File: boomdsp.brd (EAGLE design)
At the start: 100 x 100 mm, 25 parts, among them J1 RCA, J2 RCA

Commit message: proto
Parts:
- removed C1, C2: 2.2nF 50V, rcl:C025-030X050
- removed GPIO: 1X4, headers(2mm):1X4
- removed J1, J2: RCA, SparkFun-Connectors:RCA
- added OUTL, OUTR: 1X2, headers(2mm):1X2
- added U$3: 1X5, headers(2mm):1X5
- moved C14 39.5 mm to (22.5, 4.50)
- moved C13 18.7 mm to (8.50, 4.50), turned to 180 degrees
- moved R1 3.00 mm to (13.5, 9.00)
- moved C5 1.00 mm to (14.5, 13.0)
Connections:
- new net N$21: U$1.25, U$3.5
- net GND: now also C13.2, C14.2, OUTL.1, OUTR.2; no longer C1.2, C2.2
- net N$10: now also U$3.3; no longer GPIO.3
- net N$11: now also U$3.1; no longer GPIO.1
- net N$3: now also C14.1, OUTR.1; no longer C2.1
- net N$4: now also C13.1, OUTL.2; no longer C1.1
- net N$7: now also U$3.2; no longer GPIO.2
- net N$8: now also U$3.4; no longer GPIO.4
- net VDD: no longer U$1.25
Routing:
- net N$10: track 7.16 -> 1.86 mm
- net N$8: track 4.97 -> 0.60 mm
- net N$11: track 7.60 -> 4.06 mm
- net N$7: track 3.83 -> 1.32 mm
- net N$1: track 7.44 -> 9.83 mm
- net N$4: track 5.70 -> 3.55 mm
- net N$3: track 5.70 -> 3.71 mm
- net VDD: track 12.4 -> 11.3 mm

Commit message: finished prototype
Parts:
- removed C10, C11: 1uF, rcl:C0805
- removed C12: (no value), rcl:C0603K
- removed C9: 10uF 16V, rcl:153CLV-0405
- removed LED1: (no value), led:LED3MM
- removed U$3: 1X5, headers(2mm):1X5
- added C1: (no value), rcl:E3,5-8
- added POWER1: 1X2, headers(2mm):1X2
- added U$4: 1X1, headers(2mm):1X1
- U$2: value LP5907 -> 1X4; device boomdsp:SOT23-6 -> headers(2mm):1X4
- moved U$2 18.8 mm to (23.0, 26.5), turned to 270 degrees
- moved C4 5.83 mm to (7.50, 27.0)
- moved C3 5.00 mm to (11.5, 28.0)
- moved C5 4.24 mm to (11.5, 16.0)
- moved C6 4.24 mm to (9.50, 21.0)
- moved C7 4.24 mm to (11.5, 18.0)
- moved I2C 4.24 mm to (23.0, 20.5)
- moved I2S 4.24 mm to (17.5, 31.0)
- moved R1 4.24 mm to (10.5, 12.0)
- moved R2 4.24 mm to (15.5, 12.0)
- moved U$1 4.24 mm to (15.7, 22.8)
- moved C8 3.91 mm to (18.0, 16.5)
- moved C13 2.24 mm to (7.50, 6.50)
- moved OUTL 2.06 mm to (11.5, 3.00)
- moved OUTR 2.06 mm to (18.5, 3.00)
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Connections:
- removed net +5V: C10.1, POWER.1, U$2.1, U$2.3
- removed net VDD: C4.1, U$1.18, U$1.28
- net GND: now also C1.-, POWER1.2, U$1.16, U$1.24; no longer C10.2, C11.2, C9.-, U$2.2
- net N$10: now also U$2.3; no longer U$3.3
- net N$11: now also U$2.1; no longer U$3.1
- net N$15: now also C1.+; no longer C9.+
- net N$21: now also U$4.1; no longer U$3.5
- net N$7: now also U$2.2; no longer U$3.2
- net N$8: now also U$2.4; no longer U$3.4
- net VCC: now also C4.1, POWER.1, POWER1.1, U$1.18, U$1.28; no longer C11.1, U$2.6
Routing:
- net VCC: track 20.8 -> 39.2 mm
- net +5V: track 18.2 -> 0.00 mm
- net VDD: track 11.3 -> 0.00 mm
- net N$21: track 0.00 -> 6.10 mm
- net N$10: track 1.86 -> 7.16 mm
- net N$4: track 3.55 -> 8.74 mm
- net N$3: track 3.71 -> 8.68 mm
- net N$8: track 0.60 -> 4.97 mm
- net N$11: track 4.06 -> 7.60 mm
- net GND: track 7.82 -> 4.34 mm
- net N$7: track 1.32 -> 3.83 mm
- net N$15: track 6.88 -> 9.00 mm
- added copper zone on layer 16, net GND

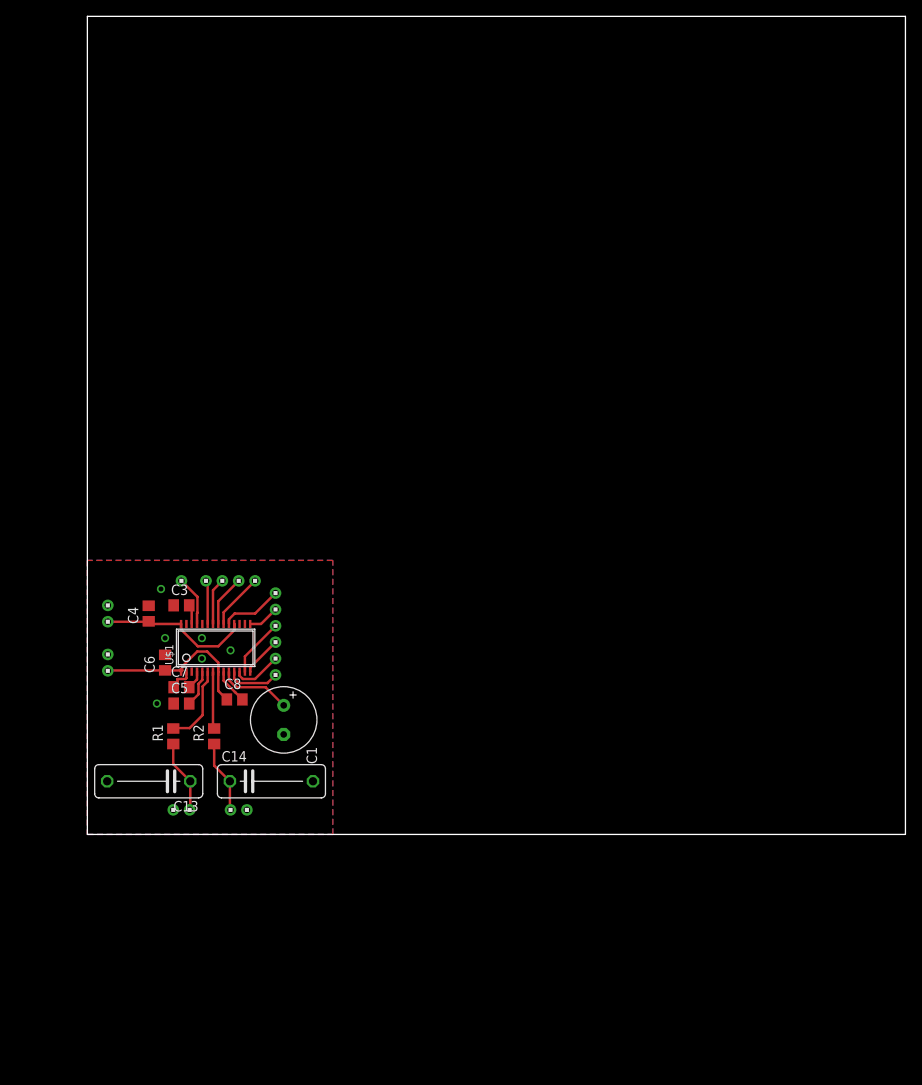
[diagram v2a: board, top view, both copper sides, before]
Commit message: via under chip. doesnt work for diy
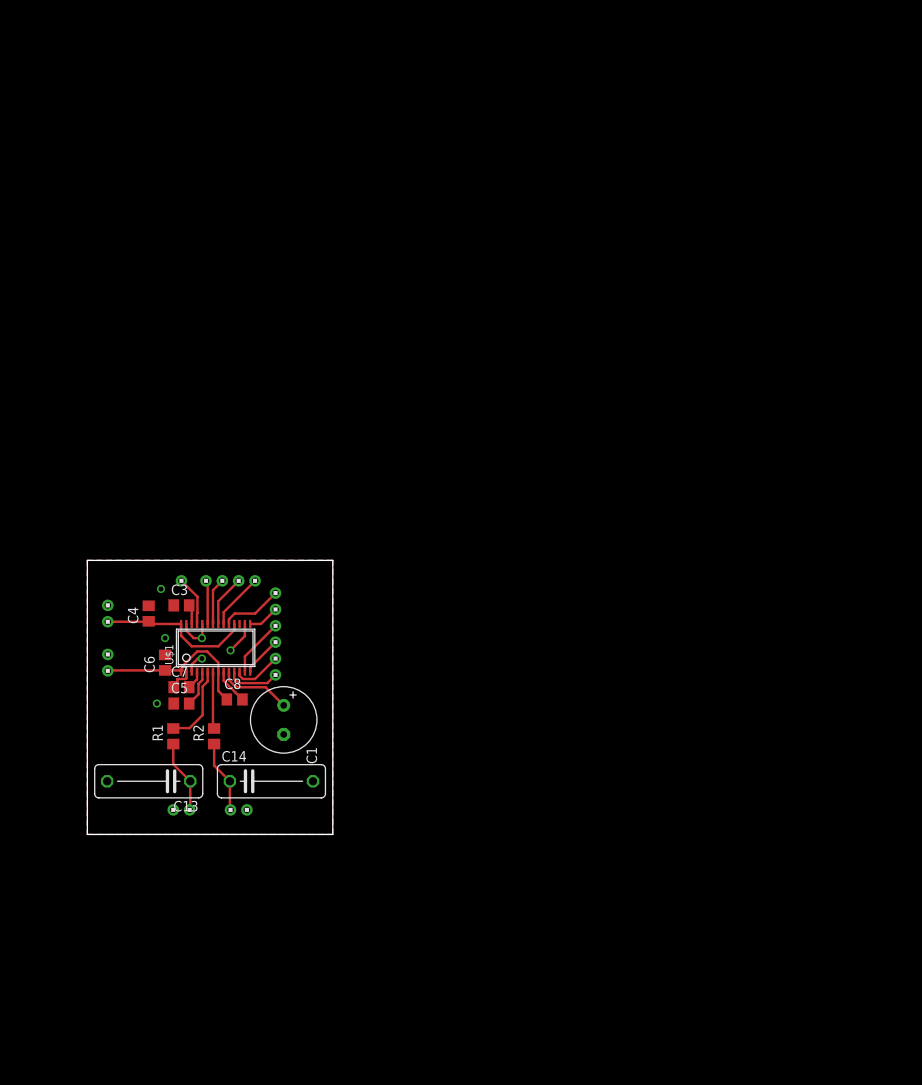
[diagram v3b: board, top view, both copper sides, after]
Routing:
- net GND: track 4.34 -> 15.6 mm
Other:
- board size 100 x 100 mm -> 30 x 33.5 mm
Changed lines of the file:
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@@
 <?xml version="1.0" encoding="utf-8"?>
 <!DOCTYPE eagle SYSTEM "eagle.dtd">
-<eagle version="8.1.0">
+<eagle version="7.6.0">
 <drawing>
 <settings>
@@
 <setting verticaltext="up"/>
 </settings>
-<grid distance="0.5" unitdist="mm" unit="mm" style="lines" multiple="1" display="no" altdistance="0.025" altunitdist="inch" altunit="inch"/>
+<grid distance="0.25" unitdist="mm" unit="mm" style="lines" multiple="1" display="no" altdistance="0.025" altunitdist="inch" altunit="inch"/>
 <layers>
 <layer number="1" name="Top" color="4" fill="1" visible="yes" active="yes"/>
@@
 <layer number="27" name="tValues" color="7" fill="1" visible="yes" active="yes"/>
 <layer number="28" name="bValues" color="7" fill="1" visible="yes" active="yes"/>
-<layer number="29" name="tStop" color="7" fill="3" visible="no" active="yes"/>
-<layer number="30" name="bStop" color="7" fill="6" visible="no" active="yes"/>
-<layer number="31" name="tCream" color="7" fill="4" visible="no" active="yes"/>
-<layer number="32" name="bCream" color="7" fill="5" visible="no" active="yes"/>
-<layer number="33" name="tFinish" color="6" fill="3" visible="no" active="yes"/>
-<layer number="34" name="bFinish" color="6" fill="6" visible="no" active="yes"/>
-<layer number="35" name="tGlue" color="7" fill="4" visible="no" active="yes"/>
-<layer number="36" name="bGlue" color="7" fill="5" visible="no" active="yes"/>
-<layer number="37" name="tTest" color="7" fill="1" visible="no" active="yes"/>
-<layer number="38" name="bTest" color="7" fill="1" visible="no" active="yes"/>
+<layer number="29" name="tStop" color="7" fill="3" visible="yes" active="yes"/>
+<layer number="30" name="bStop" color="7" fill="6" visible="yes" active="yes"/>
+<layer number="31" name="tCream" color="7" fill="4" visible="yes" active="yes"/>
+<layer number="32" name="bCream" color="7" fill="5" visible="yes" active="yes"/>
+<layer number="33" name="tFinish" color="6" fill="3" visible="yes" active="yes"/>
+<layer number="34" name="bFinish" color="6" fill="6" visible="yes" active="yes"/>
+<layer number="35" name="tGlue" color="7" fill="4" visible="yes" active="yes"/>
+<layer number="36" name="bGlue" color="7" fill="5" visible="yes" active="yes"/>
+<layer number="37" name="tTest" color="7" fill="1" visible="yes" active="yes"/>
+<layer number="38" name="bTest" color="7" fill="1" visible="yes" active="yes"/>
 <layer number="39" name="tKeepout" color="4" fill="11" visible="yes" active="yes"/>
 <layer number="40" name="bKeepout" color="1" fill="11" visible="yes" active="yes"/>
@@
 <layer number="42" name="bRestrict" color="1" fill="10" visible="yes" active="yes"/>
 <layer number="43" name="vRestrict" color="2" fill="10" visible="yes" active="yes"/>
-<layer number="44" name="Drills" color="7" fill="1" visible="no" active="yes"/>
-<layer number="45" name="Holes" color="7" fill="1" visible="no" active="yes"/>
-<layer number="46" name="Milling" color="3" fill="1" visible="no" active="yes"/>
-<layer number="47" name="Measures" color="7" fill="1" visible="no" active="yes"/>
+<layer number="44" name="Drills" color="7" fill="1" visible="yes" active="yes"/>
+<layer number="45" name="Holes" color="7" fill="1" visible="yes" active="yes"/>
+<layer number="46" name="Milling" color="3" fill="1" visible="yes" active="yes"/>
+<layer number="47" name="Measures" color="7" fill="1" visible="yes" active="yes"/>
 <layer number="48" name="Document" color="7" fill="1" visible="yes" active="yes"/>
 <layer number="49" name="Reference" color="7" fill="1" visible="yes" active="yes"/>
@@
 <board>
 <plain>
-<wire x1="0" y1="0" x2="100" y2="0" width="0" layer="20"/>
-<wire x1="100" y1="0" x2="100" y2="100" width="0" layer="20"/>
-<wire x1="100" y1="100" x2="0" y2="100" width="0" layer="20"/>
-<wire x1="0" y1="100" x2="0" y2="0" width="0" layer="20"/>
+<wire x1="0" y1="0" x2="30" y2="0" width="0" layer="20"/>
+<wire x1="30" y1="0" x2="30" y2="33.5" width="0" layer="20"/>
+<wire x1="30" y1="33.5" x2="0" y2="33.5" width="0" layer="20"/>
+<wire x1="0" y1="33.5" x2="0" y2="0" width="0" layer="20"/>
 </plain>
 <attributes>
@@
 <contactref element="C6" pad="2"/>
 <contactref element="U$1" pad="3"/>
-<polygon width="0.3048" layer="1">
+<polygon width="0.3048" layer="1" isolate="0.4064">
 <vertex x="0" y="0"/>
 <vertex x="30" y="0"/>
@@
 <wire x1="16.655" y1="19.8922" x2="16.655" y2="18.79789375" width="0.3048" layer="1"/>
 <wire x1="16.655" y1="18.79789375" x2="18.0556" y2="17.39729375" width="0.3048" layer="1"/>
-<polygon width="0.3048" layer="16">
+<polygon width="0.3048" layer="16" isolate="0.6096">
 <vertex x="0" y="0"/>
 <vertex x="30" y="0"/>
@@
 <vertex x="0" y="33.5"/>
 </polygon>
+<wire x1="12.105" y1="25.7278" x2="12.105" y2="24.895" width="0.3048" layer="1"/>
+<wire x1="12.105" y1="24.895" x2="13" y2="24" width="0.3048" layer="1"/>
+<wire x1="13" y1="24" x2="14" y2="24" width="0.3048" layer="1"/>
+<wire x1="14.055" y1="25.7278" x2="14.055" y2="24.055" width="0.3048" layer="1"/>
+<wire x1="14.055" y1="24.055" x2="14" y2="24" width="0.3048" layer="1"/>
+<wire x1="19.255" y1="25.7278" x2="19.255" y2="24.255" width="0.3048" layer="1"/>
+<wire x1="19.255" y1="24.255" x2="17.5" y2="22.5" width="0.3048" layer="1"/>
+<wire x1="14" y1="21.5" x2="13.5" y2="21.5" width="0.3048" layer="1"/>
+<wire x1="13.5" y1="21.5" x2="12.75" y2="20.75" width="0.3048" layer="1"/>
+<wire x1="12.75" y1="20.75" x2="12.75" y2="19.8972" width="0.3048" layer="1"/>
+<wire x1="12.75" y1="19.8972" x2="12.755" y2="19.8922" width="0.3048" layer="1"/>
 </signal>
 <signal name="VCC">
@@
 <contactref element="U$1" pad="28"/>
 <contactref element="U$1" pad="18"/>
-<wire x1="11.455" y1="25.045" x2="11.455" y2="25.7278" width="0.3048" layer="1"/>
-<wire x1="11.455" y1="25.045" x2="13.5" y2="23" width="0.3048" layer="1"/>
-<wire x1="16" y1="23" x2="13.5" y2="23" width="0.3048" layer="1"/>
+<wire x1="16" y1="23" x2="12.75" y2="23" width="0.3048" layer="1"/>
 <wire x1="16" y1="23" x2="18" y2="25" width="0.3048" layer="1"/>
 <wire x1="18" y1="25" x2="18" y2="25.6828" width="0.3048" layer="1"/>
@@
 <wire x1="2.5" y1="26" x2="7.45" y2="26" width="0.3048" layer="1"/>
 <wire x1="7.45" y1="26" x2="7.5" y2="26.05" width="0.3048" layer="1"/>
-<wire x1="13.42100625" y1="22.3588" x2="13.5" y2="23" width="0" layer="19" extent="1-1"/>
+<wire x1="11.455" y1="25.7278" x2="11.455" y2="24.295" width="0.3048" layer="1"/>
+<wire x1="11.455" y1="24.295" x2="12.75" y2="23" width="0.3048" layer="1"/>
+<wire x1="13.42100625" y1="22.3588" x2="12.75" y2="23" width="0" layer="19" extent="1-1"/>
 </signal>
 <signal name="N$7">
